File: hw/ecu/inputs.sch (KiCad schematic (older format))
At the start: 103 parts, among them J10 CUR_LOOP_IN, J11 SENSORS, J8 BUTTONS, J9 ENGINE, U6 74HC4050, U7 74HC4050

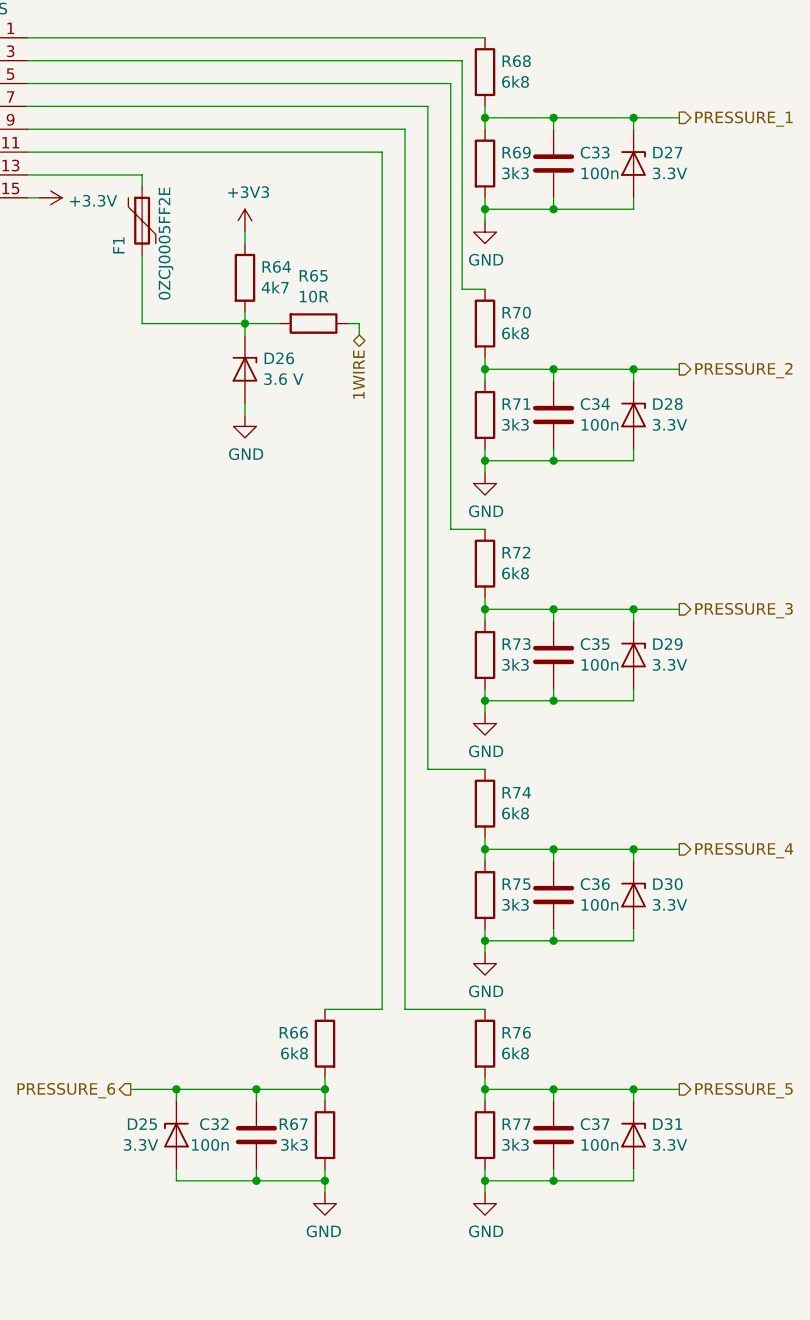
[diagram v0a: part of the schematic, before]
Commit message: Updated few resistors/capacitors values on board
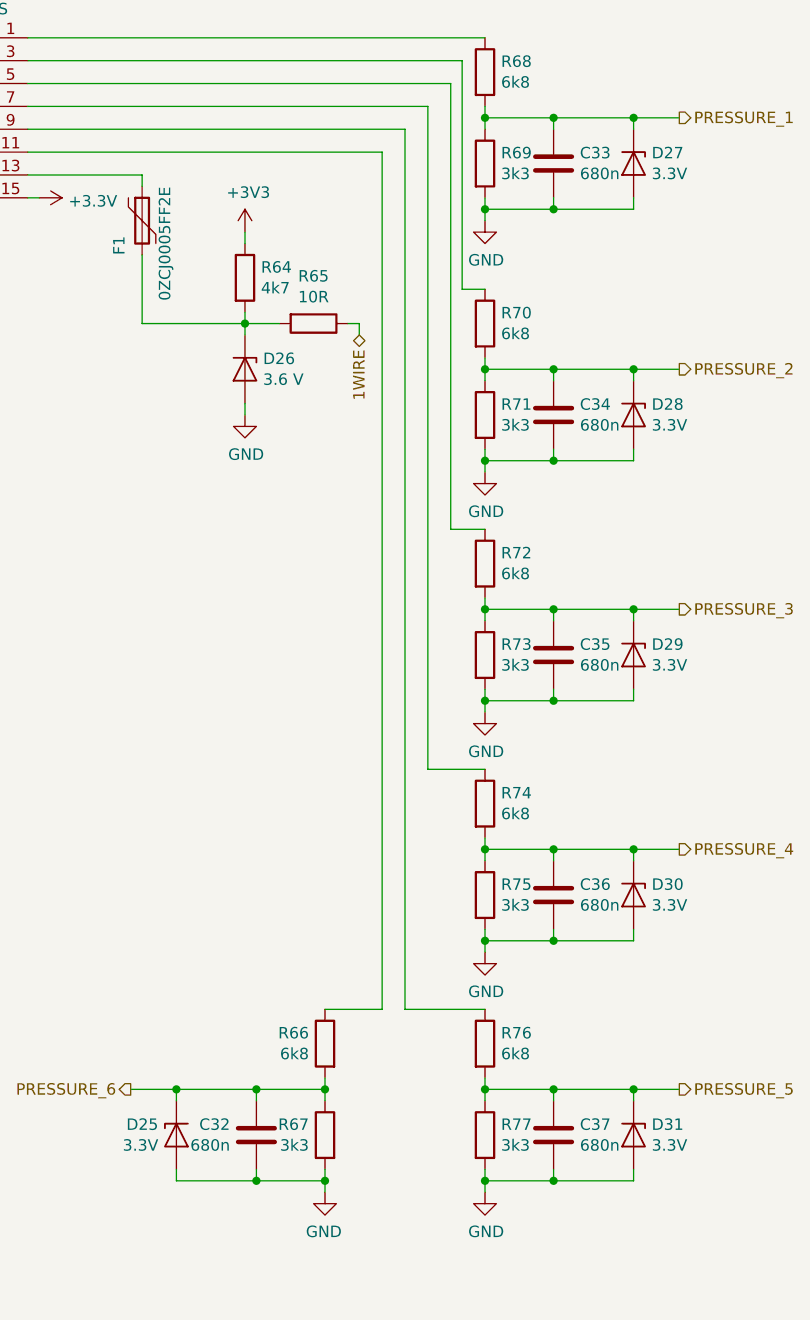
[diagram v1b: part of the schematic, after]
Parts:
- C32, C33, C34, C35, C36, C37: value 100n -> 680n
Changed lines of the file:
@@
 AR Path="/5F2321E1/5F2F70F7" Ref="C33"  Part="1"
 F 0 "C33" H 10165 1496 50  0000 L CNN
-F 1 "100n" H 10165 1405 50  0000 L CNN
+F 1 "680n" H 10165 1405 50  0000 L CNN
 F 2 "Capacitor_SMD:C_0805_2012Metric" H 10088 1300 50  0001 C CNN
 F 3 "~" H 10050 1450 50  0001 C CNN
@@
 AR Path="/5F2321E1/5F8B52E6" Ref="C34"  Part="1"
 F 0 "C34" H 10165 2596 50  0000 L CNN
-F 1 "100n" H 10165 2505 50  0000 L CNN
+F 1 "680n" H 10165 2505 50  0000 L CNN
 F 2 "Capacitor_SMD:C_0805_2012Metric" H 10088 2400 50  0001 C CNN
 F 3 "~" H 10050 2550 50  0001 C CNN
@@
 AR Path="/5F2321E1/5F8D8C80" Ref="C35"  Part="1"
 F 0 "C35" H 10165 3646 50  0000 L CNN
-F 1 "100n" H 10165 3555 50  0000 L CNN
+F 1 "680n" H 10165 3555 50  0000 L CNN
 F 2 "Capacitor_SMD:C_0805_2012Metric" H 10088 3450 50  0001 C CNN
 F 3 "~" H 10050 3600 50  0001 C CNN
@@
 AR Path="/5F2321E1/600844DB" Ref="C36"  Part="1"
 F 0 "C36" H 10165 4696 50  0000 L CNN
-F 1 "100n" H 10165 4605 50  0000 L CNN
+F 1 "680n" H 10165 4605 50  0000 L CNN
 F 2 "Capacitor_SMD:C_0805_2012Metric" H 10088 4500 50  0001 C CNN
 F 3 "~" H 10050 4650 50  0001 C CNN
@@
 AR Path="/5F2321E1/6009A9A4" Ref="C37"  Part="1"
 F 0 "C37" H 10165 5746 50  0000 L CNN
-F 1 "100n" H 10165 5655 50  0000 L CNN
+F 1 "680n" H 10165 5655 50  0000 L CNN
 F 2 "Capacitor_SMD:C_0805_2012Metric" H 10088 5550 50  0001 C CNN
 F 3 "~" H 10050 5700 50  0001 C CNN
@@
 AR Path="/5F2321E1/60478624" Ref="C32"  Part="1"
 F 0 "C32" H 8865 5746 50  0000 L CNN
-F 1 "100n" H 8865 5655 50  0000 L CNN
+F 1 "680n" H 8865 5655 50  0000 L CNN
 F 2 "Capacitor_SMD:C_0805_2012Metric" H 8788 5550 50  0001 C CNN
 F 3 "~" H 8750 5700 50  0001 C CNN

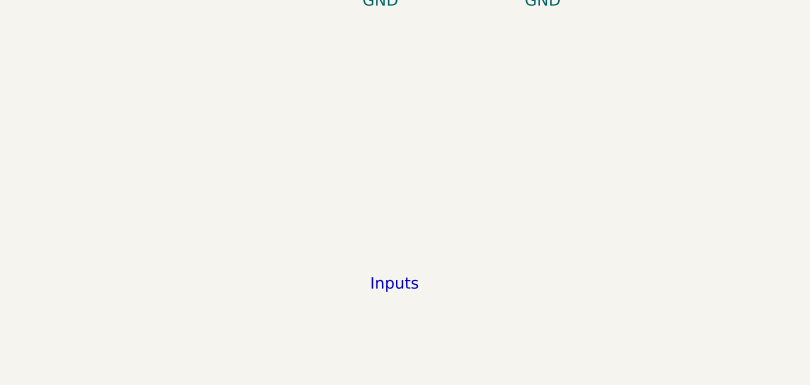
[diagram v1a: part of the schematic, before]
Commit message: Added schematics for all parts
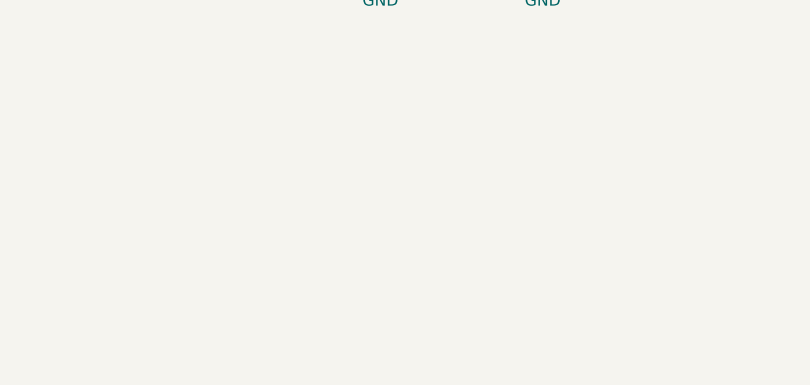
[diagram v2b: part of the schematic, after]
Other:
- note removed: "Inputs"
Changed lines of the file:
@@
 	0    1    1    0
 $EndComp
-Text Notes 9000 7400 0    50   ~ 0
-Inputs
 $Comp
 L 4xxx:4050 U?

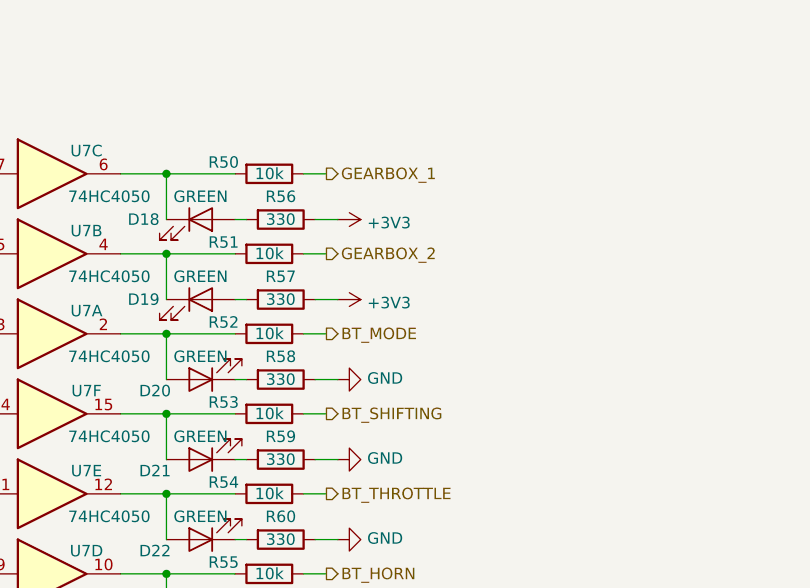
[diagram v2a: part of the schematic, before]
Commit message: Added crystal for all can equipped boards
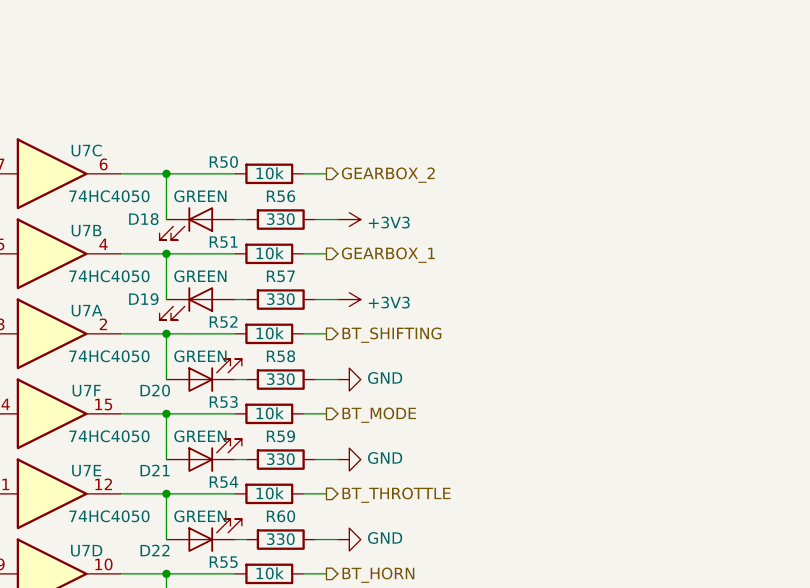
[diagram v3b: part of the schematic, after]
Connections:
- net BT_MODE: now also R53.1; no longer R52.1
- net BT_SHIFTING: now also R52.1; no longer R53.1
- net GEARBOX_1: now also R51.1; no longer R50.1
- net GEARBOX_2: now also R50.1; no longer R51.1
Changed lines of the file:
@@
 Sheet 2 7
 Title "BUT Pneumobil - ECU inputs"
-Date "2018-10-04"
-Rev "0.1"
+Date "2019-03-11"
+Rev "0.2"
 Comp "Brno University of Technology"
 Comment1 "Jakub Kaderka"
@@
 	1    0    0    -1
 $EndComp
+Text HLabel 5550 4800 2    50   Output ~ 0
+GEARBOX_1
 Text HLabel 5550 4450 2    50   Output ~ 0
-GEARBOX_1
-Text HLabel 5550 4800 2    50   Output ~ 0
 GEARBOX_2
 $Comp
@@
 	0    1    1    0
 $EndComp
+Text HLabel 5550 5500 2    50   Output ~ 0
+BT_MODE
 Text HLabel 5550 5150 2    50   Output ~ 0
-BT_MODE
-Text HLabel 5550 5500 2    50   Output ~ 0
 BT_SHIFTING
 Wire Wire Line
@@
 Connection ~ 4850 5500
 Wire Wire Line
+	5450 5150 5550 5150
+Wire Wire Line
+	5500 4650 5600 4650
+Wire Wire Line
+	5450 4800 5550 4800
+Wire Wire Line
+	5500 5000 5600 5000
+Wire Wire Line
 	5450 4450 5550 4450
 Wire Wire Line
-	5500 4650 5600 4650
-Wire Wire Line
-	5450 4800 5550 4800
-Wire Wire Line
-	5500 5000 5600 5000
-Wire Wire Line
-	5450 5150 5550 5150
-Wire Wire Line
 	5450 5500 5550 5500

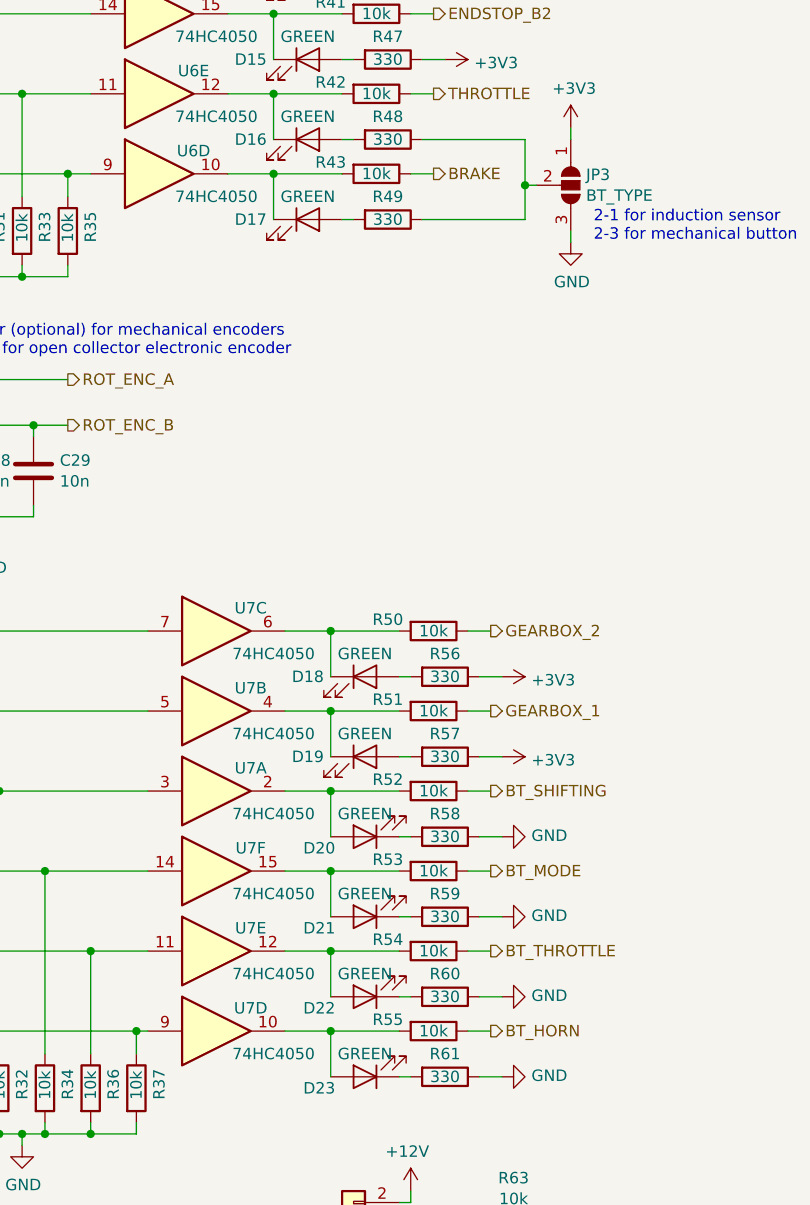
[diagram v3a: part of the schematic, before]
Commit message: Reduced resistors for horn and brake buttons to switch on mosfets
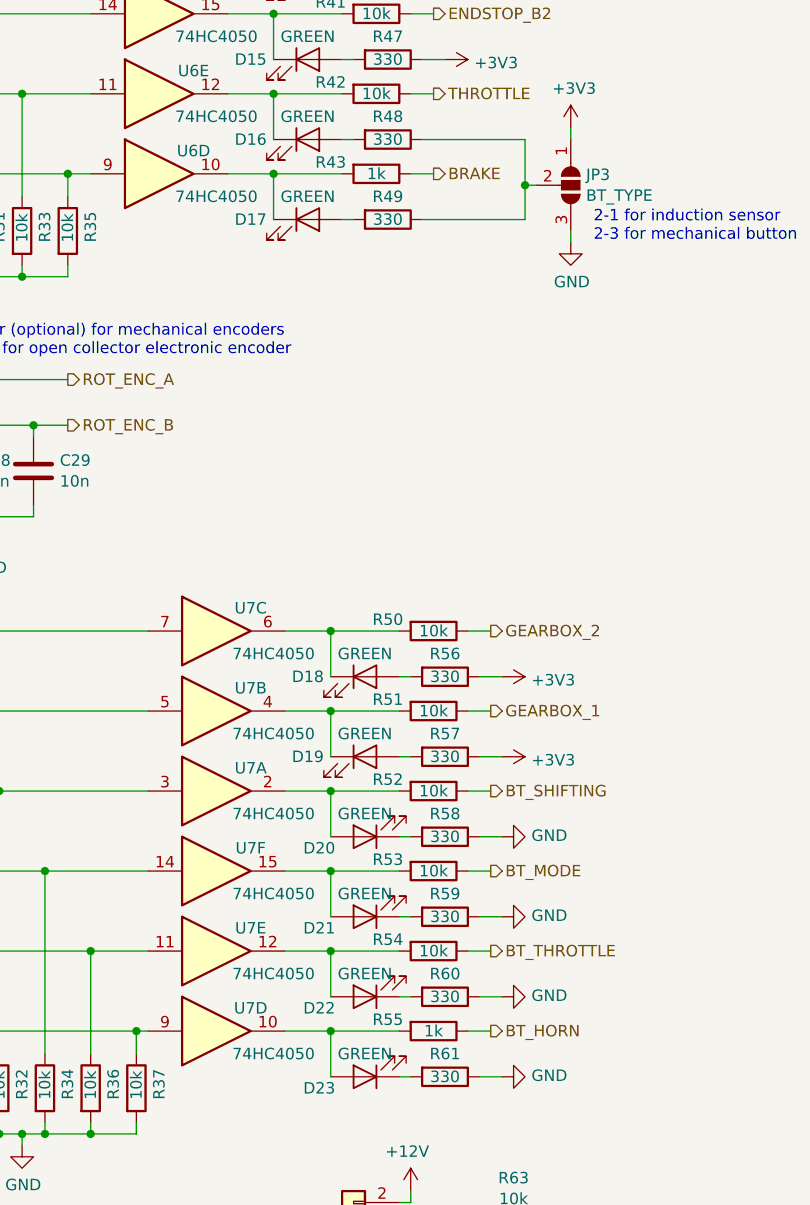
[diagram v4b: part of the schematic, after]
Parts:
- R43, R55: value 10k -> 1k
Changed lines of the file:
@@
 P 5050 2450
 F 0 "R43" V 5000 2250 50  0000 C CNN
-F 1 "10k" V 5050 2450 50  0000 C CNN
+F 1 "1k" V 5050 2450 50  0000 C CNN
 F 2 "Resistor_SMD:R_0805_2012Metric" V 4980 2450 50  0001 C CNN
 F 3 "~" H 5050 2450 50  0001 C CNN
@@
 P 5300 6200
 F 0 "R55" V 5250 6000 50  0000 C CNN
-F 1 "10k" V 5300 6200 50  0000 C CNN
+F 1 "1k" V 5300 6200 50  0000 C CNN
 F 2 "Resistor_SMD:R_0805_2012Metric" V 5230 6200 50  0001 C CNN
 F 3 "~" H 5300 6200 50  0001 C CNN
